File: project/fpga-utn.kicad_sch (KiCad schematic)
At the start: 0 parts

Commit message: Regulador V1 finalizado
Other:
- sheet Power Supply ports: added 1V2, 3V3, 5V, D+, D-, GND; removed none
- note added: "Basado en LDO"
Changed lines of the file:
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@@
 	(generator_version "8.0")
 	(paper "A4")
+	(text "Basado en LDO"
+		(exclude_from_sim no)
+		(at 66.548 69.85 0)
+		(effects
+			(font
+				(size 2.55 2.55)
+				(thickness 0.51)
+				(bold yes)
+			)
+		)
+	)
 	(text "Aqui se inicia nuestro proyecto final"
 		(exclude_from_sim no)
@@
 	)
 	(sheet
-		(at 30.48 46.99)
+		(at 34.29 46.99)
 		(size 63.5 44.45)
 		(stroke
@@
 		)
 		(property "Sheetname" "Power Supply"
-			(at 30.48 46.2784 0)
+			(at 34.29 46.2784 0)
 			(effects
 				(font
@@
 		)
 		(property "Sheetfile" "power_supply.kicad_sch"
-			(at 30.48 92.0246 0)
+			(at 34.29 92.0246 0)
 			(effects
 				(font
@@
 			)
 		)
+		(pin "D+" bidirectional
+			(at 97.79 53.34 0)
+			(effects
+				(font
+					(size 1.27 1.27)
+				)
+				(justify right)
+			)
+		)
+		(pin "D-" bidirectional
+			(at 97.79 58.42 0)
+			(effects
+				(font
+					(size 1.27 1.27)
+				)
+				(justify right)
+			)
+		)
+		(pin "1V2" output
+			(at 97.79 77.47 0)
+			(effects
+				(font
+					(size 1.27 1.27)
+				)
+				(justify right)
+			)
+		)
+		(pin "3V3" output
+			(at 97.79 71.12 0)
+			(effects
+				(font
+					(size 1.27 1.27)
+				)
+				(justify right)
+			)
+		)
+		(pin "GND" output
+			(at 97.79 85.09 0)
+			(effects
+				(font
+					(size 1.27 1.27)
+				)
+				(justify right)
+			)
+		)
+		(pin "5V" output
+			(at 97.79 64.77 0)
+			(effects
+				(font
+					(size 1.27 1.27)
+				)
+				(justify right)
+			)
+		)

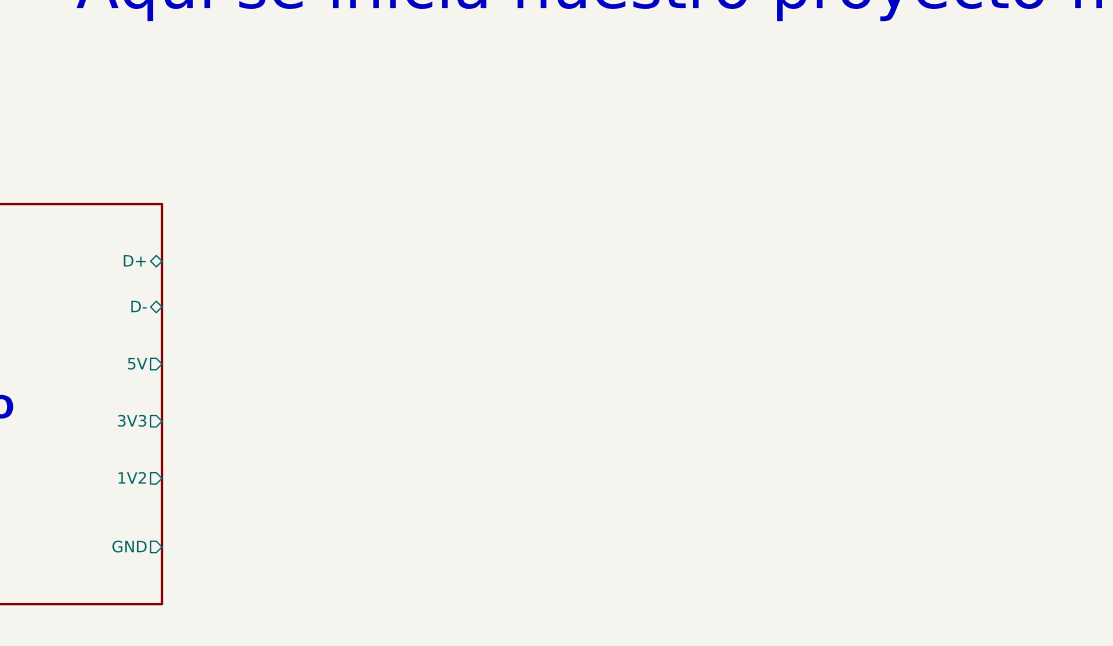
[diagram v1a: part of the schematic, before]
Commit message: Sección de FTDI casi terminada. Definir oscilador y nombres de puertos
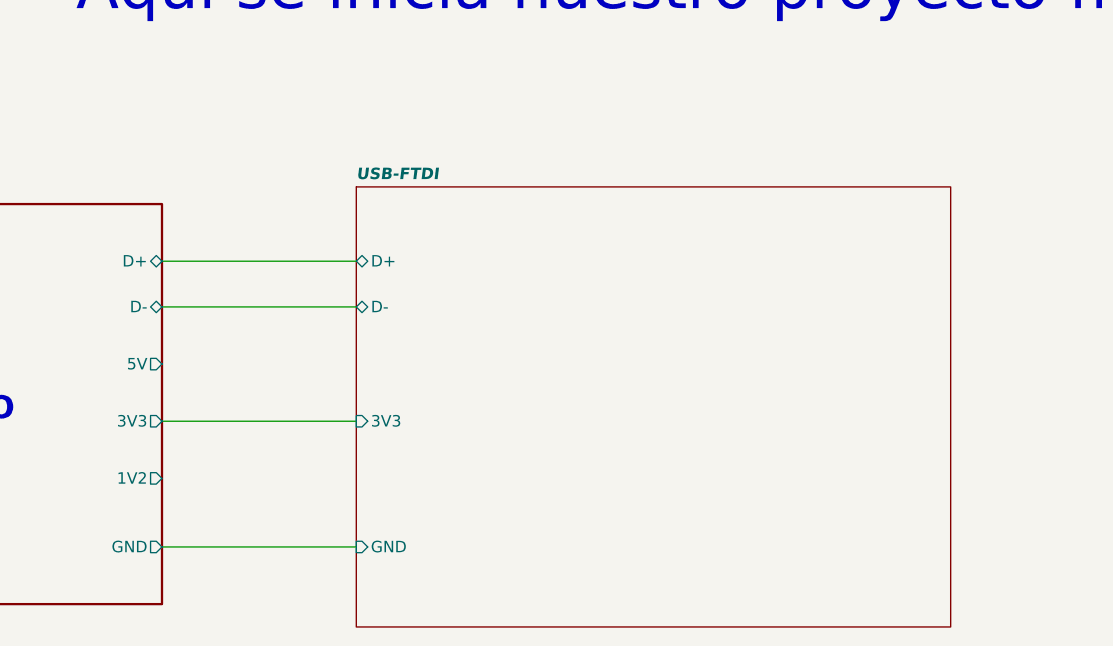
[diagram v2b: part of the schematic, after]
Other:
- added sheet USB-FTDI (FTDI.kicad_sch)
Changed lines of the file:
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@@
 	(generator_version "8.0")
 	(paper "A4")
+	(wire
+		(pts
+			(xy 97.79 85.09) (xy 119.38 85.09)
+		)
+		(stroke
+			(width 0)
+			(type default)
+		)
+	)
+	(wire
+		(pts
+			(xy 97.79 58.42) (xy 119.38 58.42)
+		)
+		(stroke
+			(width 0)
+			(type default)
+		)
+	)
+	(wire
+		(pts
+			(xy 97.79 71.12) (xy 119.38 71.12)
+		)
+		(stroke
+			(width 0)
+			(type default)
+		)
+	)
+	(wire
+		(pts
+			(xy 97.79 53.34) (xy 119.38 53.34)
+		)
+		(stroke
+			(width 0)
+			(type default)
+		)
+	)
 	(text "Basado en LDO"
 		(exclude_from_sim no)
@@
 			)
 		)
+	)
+	(sheet
+		(at 119.38 45.085)
+		(size 66.04 48.895)
+		(fields_autoplaced yes)
+		(stroke
+			(width 0.1524)
+			(type solid)
+		)
+		(fill
+			(color 0 0 0 0.0000)
+		)
+		(property "Sheetname" "USB-FTDI"
+			(at 119.38 44.3734 0)
+			(effects
+				(font
+					(size 1.27 1.27)
+					(thickness 0.254)
+					(bold yes)
+					(italic yes)
+				)
+				(justify left bottom)
+			)
+		)
+		(property "Sheetfile" "FTDI.kicad_sch"
+			(at 119.38 94.5646 0)
+			(effects
+				(font
+					(size 1.27 1.27)
+				)
+				(justify left top)
+				(hide yes)
+			)
+		)
+		(pin "D-" bidirectional
+			(at 119.38 58.42 180)
+			(effects
+				(font
+					(size 1.27 1.27)
+				)
+				(justify left)
+			)
+		)
+		(pin "3V3" input
+			(at 119.38 71.12 180)
+			(effects
+				(font
+					(size 1.27 1.27)
+				)
+				(justify left)
+			)
+		)
+		(pin "GND" input
+			(at 119.38 85.09 180)
+			(effects
+				(font
+					(size 1.27 1.27)
+				)
+				(justify left)
+			)
+		)
+		(pin "D+" bidirectional
+			(at 119.38 53.34 180)
+			(effects
+				(font
+					(size 1.27 1.27)
+				)
+				(justify left)
+			)
+		)
+		(instances
+			(project "fpga-utn"
+				(path "/fadb8841-cd7a-4174-937d-7c393e857c90"
+					(page "3")
+				)
+			)
+		)

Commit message: Guardado previo, FTDI casi listo
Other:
- added sheet FPGA (fpga.kicad_sch)
- added sheet Memorias (memorias.kicad_sch)
- sheet USB-FTDI ports: added EEPROM_CLK, EEPROM_CS, EEPROM_DATA, Flash_CS, Flash_DI, Flash_DO, Flash_DONE, Flash_RESET, Flash_SCK, VUART_CTS, VUART_DCD, VUART_DSR, VUART_DTR, VUART_RTS, VUART_Rx, VUART_Tx; removed none

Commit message: Guardado previo, FTDI casi listo
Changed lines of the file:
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@@
 	(sheet
 		(at 115.57 92.71)
-		(size 67.31 38.1)
+		(size 60.96 27.94)
 		(fields_autoplaced yes)
 		(stroke
@@
 		)
 		(property "Sheetfile" "memorias.kicad_sch"
-			(at 115.57 131.3946 0)
+			(at 115.57 121.2346 0)
 			(effects
 				(font

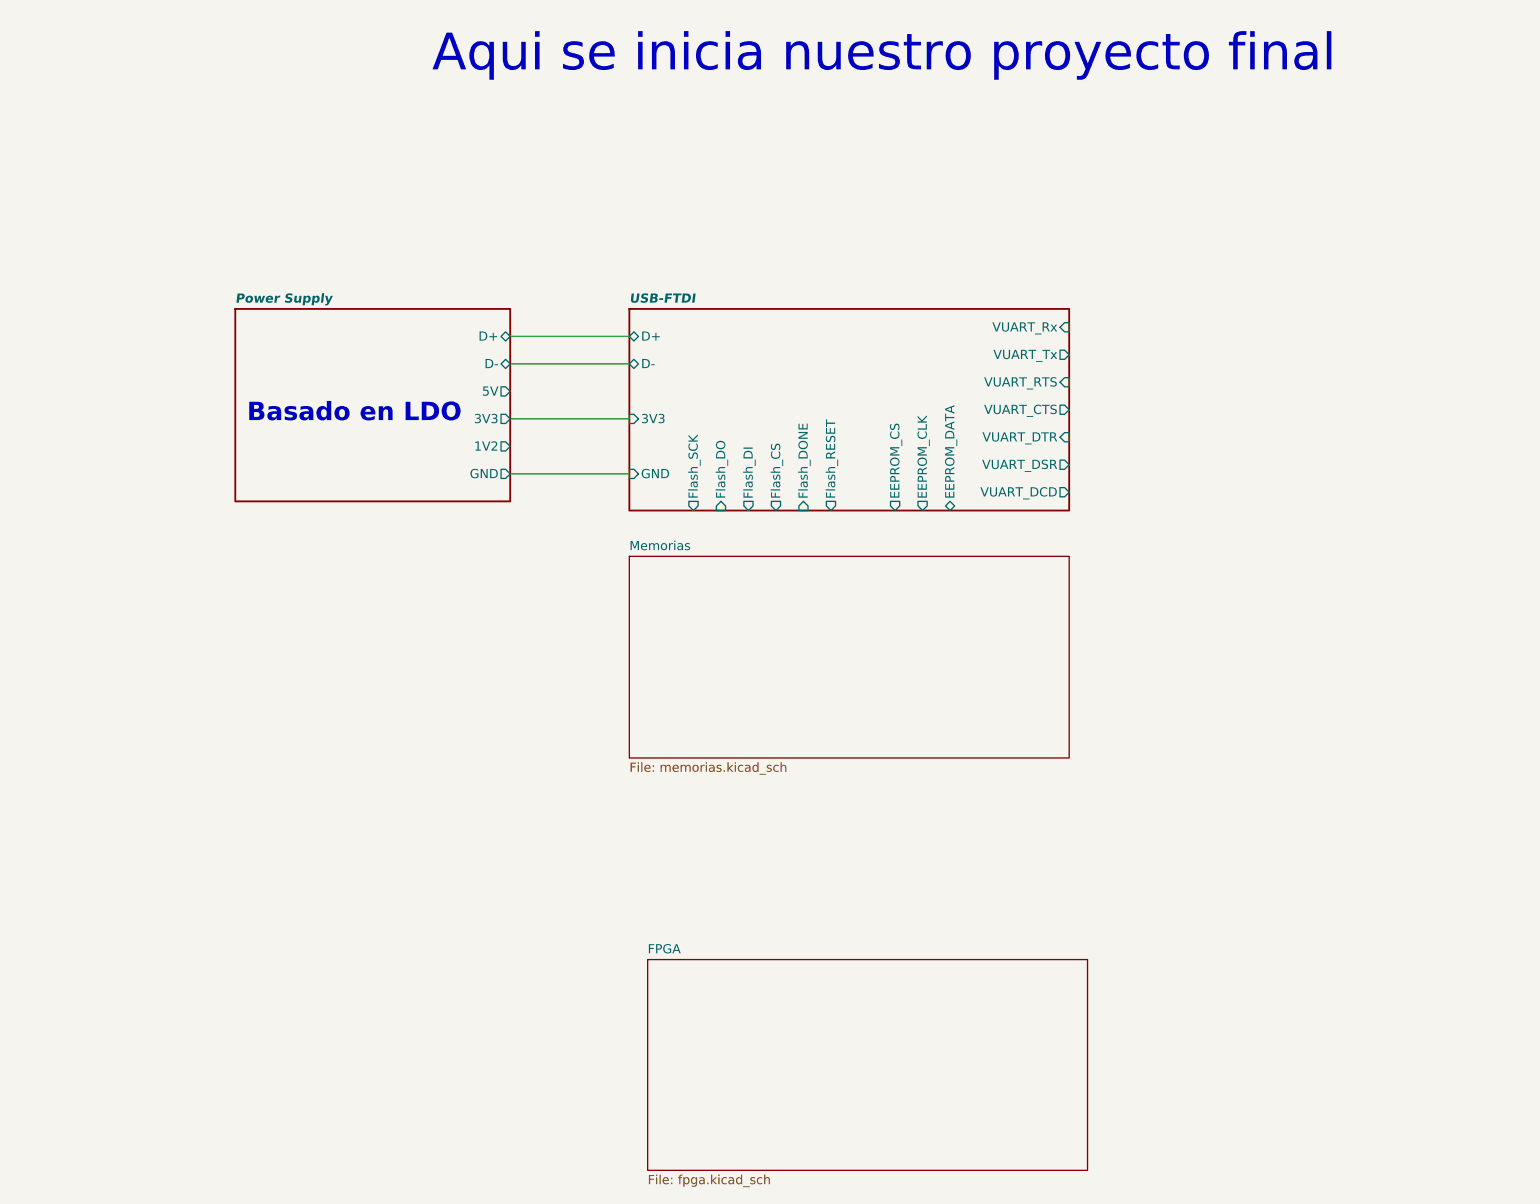
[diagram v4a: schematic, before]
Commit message: Corrigiendo errores de conexiones en la memorias
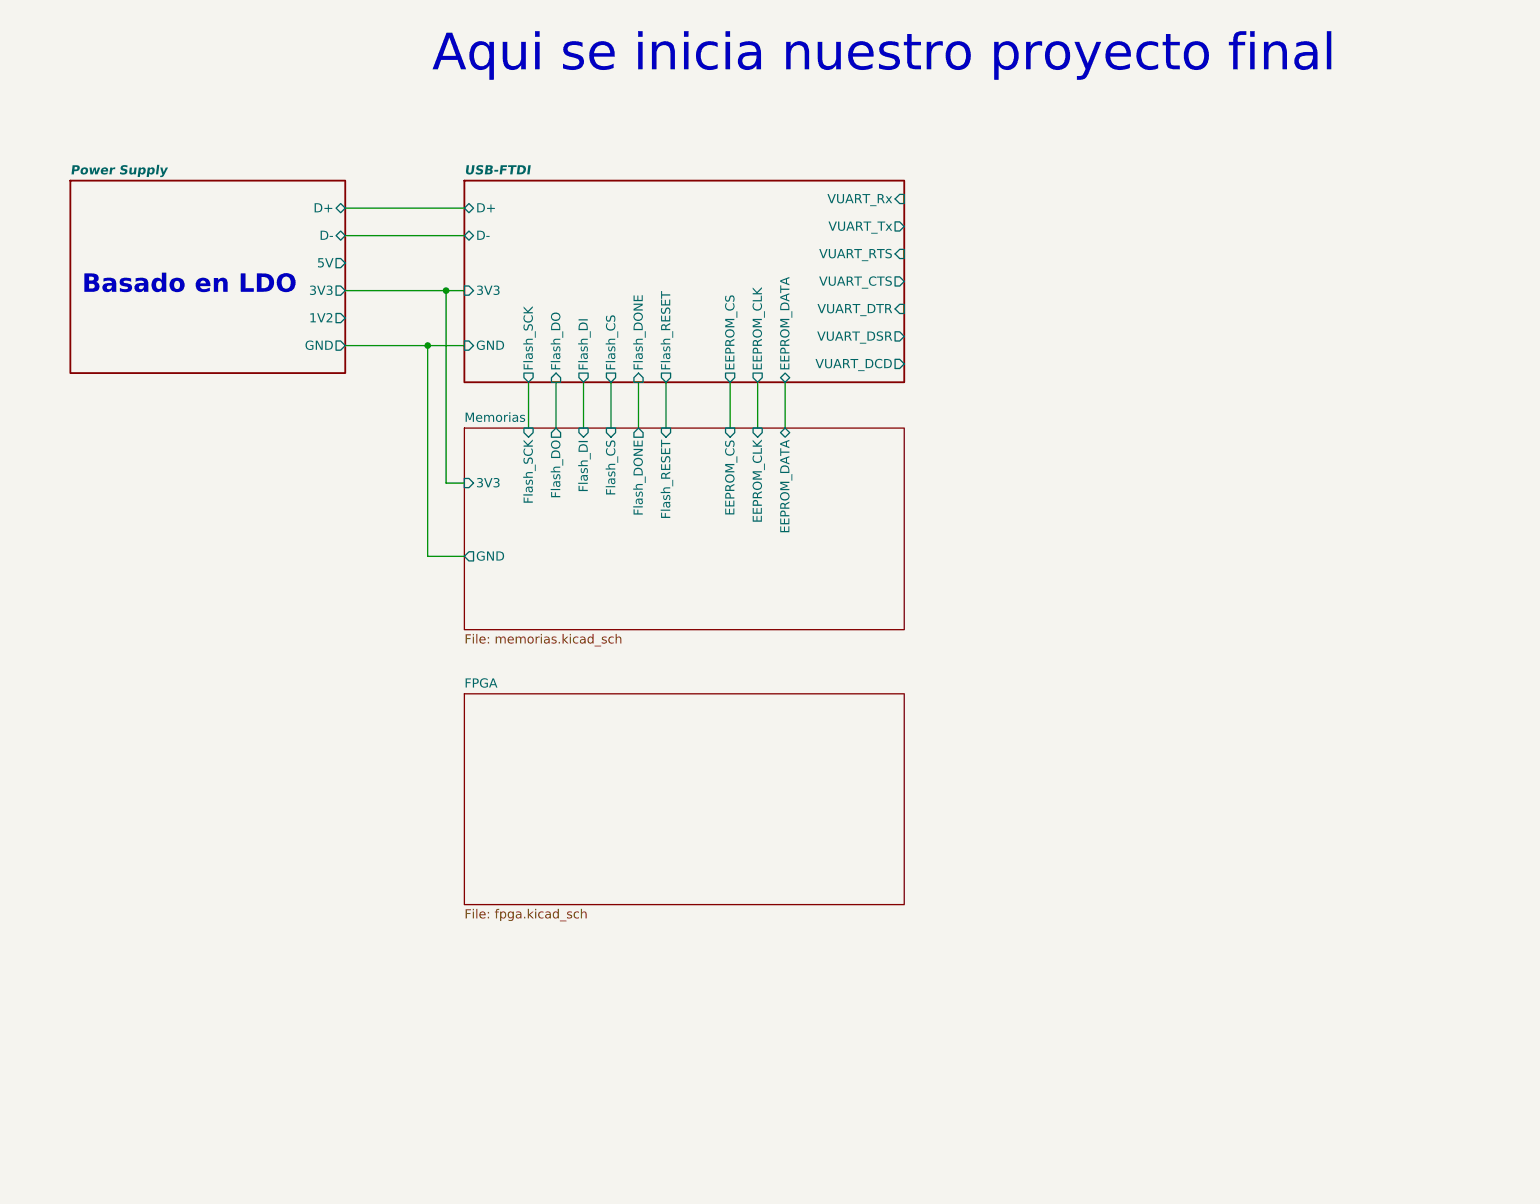
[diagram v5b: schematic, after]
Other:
- sheet Memorias ports: added 3V3, EEPROM_CLK, EEPROM_CS, EEPROM_DATA, Flash_CS, Flash_DI, Flash_DO, Flash_DONE, Flash_RESET, Flash_SCK, GND; removed none

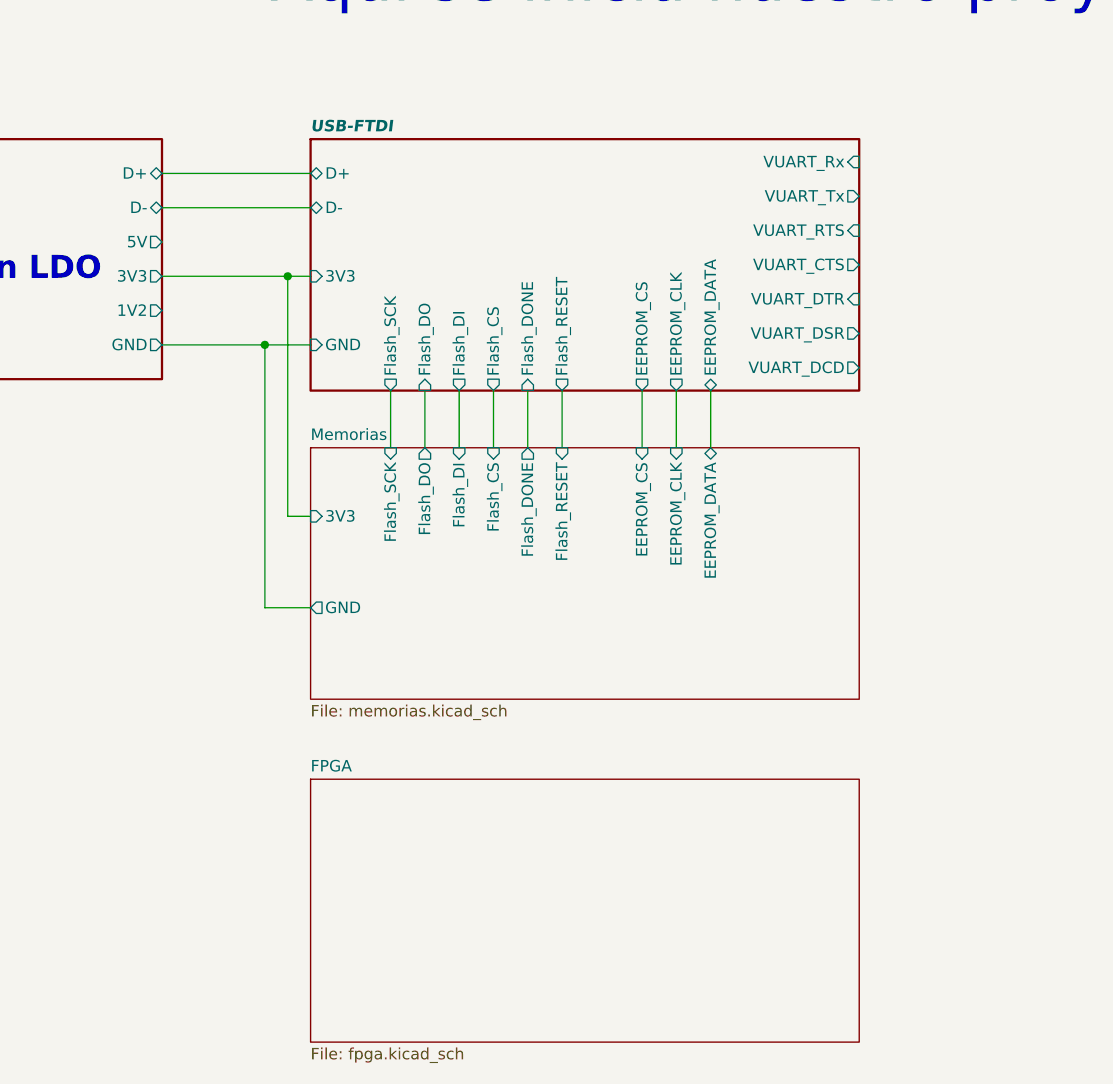
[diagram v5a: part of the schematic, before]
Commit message: Inicio de la PCB y conexion del PLL
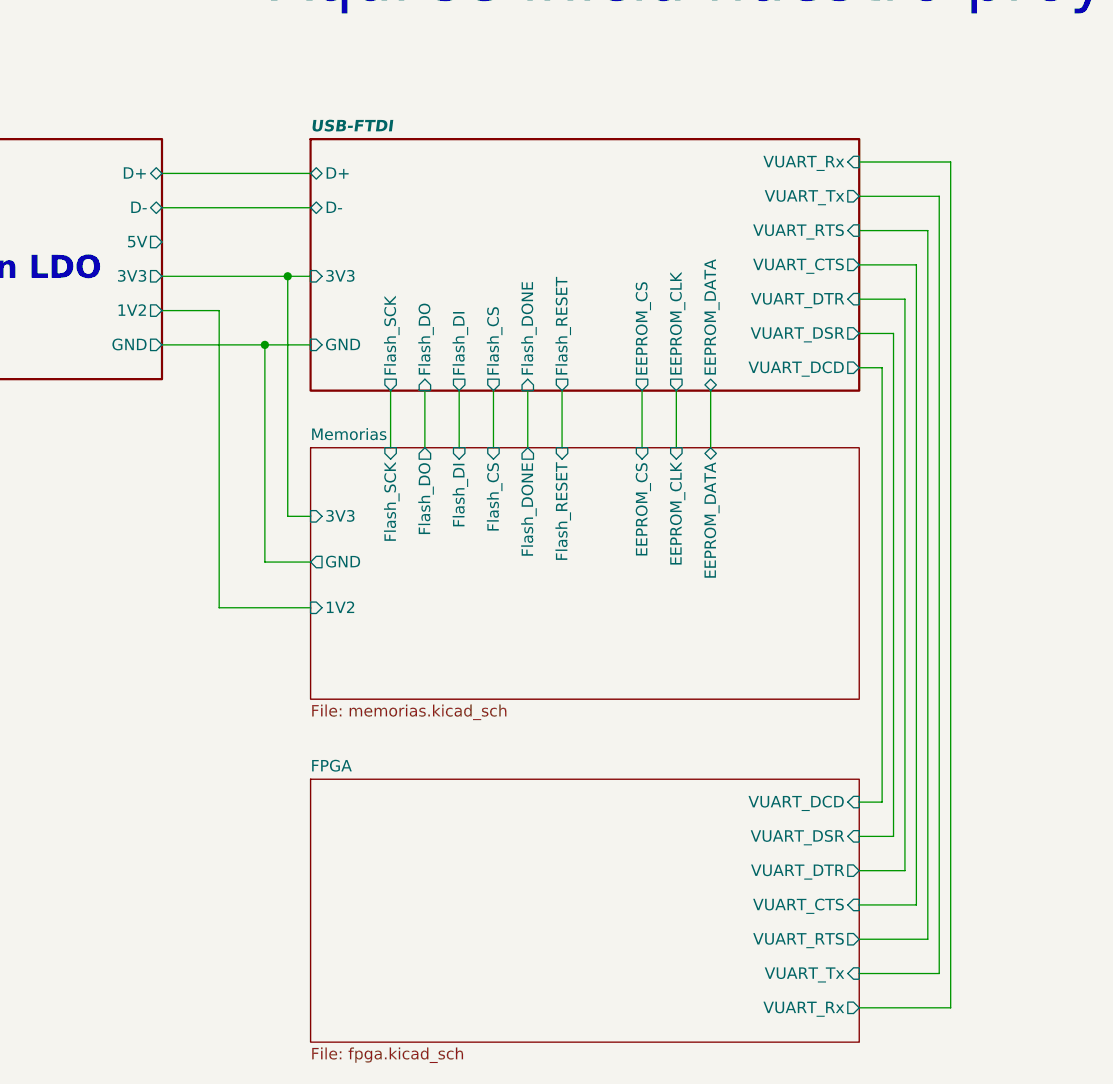
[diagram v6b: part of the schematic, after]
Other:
- sheet FPGA ports: added VUART_CTS, VUART_DCD, VUART_DSR, VUART_DTR, VUART_RTS, VUART_Rx, VUART_Tx; removed none
- sheet Memorias ports: added 1V2; removed none
